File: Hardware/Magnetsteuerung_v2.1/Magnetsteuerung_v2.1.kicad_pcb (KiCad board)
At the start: 2 copper layers, 92.1 x 100.1 mm, 222 parts, among them J1 Conn_02x08_Odd_Even, J16 OUT1, J17 OUT1, J18 OUT1, J19 OUT1, J2 OUT1, J20 OUT1, J21 OUT1, J3 Conn_01x16, J4 OUT1, J5 OUT1, J6 OUT1, J7 OUT1, J8 OUT1, J9 Conn_01x16, Q1 Q_NMOS_GSD, Q10 Q_NMOS_GSD, Q11 Q_NMOS_GSD, Q12 Q_NMOS_GSD, Q13 Q_NMOS_GSD, Q14 Q_NMOS_GSD, Q15 Q_NMOS_GSD, Q16 Q_NMOS_GSD, Q17 Q_NMOS_GDS, Q2 Q_NMOS_GSD, Q3 Q_NMOS_GSD, Q4 Q_NMOS_GSD, Q5 Q_NMOS_GSD, Q6 Q_NMOS_GSD, Q7 Q_NMOS_GSD, Q8 Q_NMOS_GSD, U1 TL2575, U10 MCP1416R, U11 MCP1416R, U12 MCP1416R, U13 MCP1416R, U14 MCP1416R, U15 MCP1416R, U16 MCP1416R, U17 MCP1416R, U2 MCP1416R, U3 MCP1416R, U4 MCP1416R, U5 MCP1416R, U6 MCP1416R, U7 MCP1416R, U8 MCP1416R, U9 MCP1416R

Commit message: Add V2.1
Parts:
- removed D32, D33, D34, D41, D42, D43, D48, D49: LED, LED_SMD:LED_0603_1608Metric
- removed F10, F11, F12, F13, F14, F15, F16, F9: Fuse, Fuse:Fuse_2920_7451Metric_Pad2.10x5.45mm_HandSolder
- removed J16, J17, J18, J19, J20, J21, J5, J6: OUT1, MK_Footprints:SPTAF_2
- removed R42, R43, R44, R54, R55, R56, R63, R64: 9.5k, Resistor_SMD:R_0603_1608Metric
- added C10: 10u, Capacitor_SMD:C_1210_3225Metric, F.Cu at (171.1, 81.0)
- added C11: 10u, Capacitor_SMD:C_1210_3225Metric, F.Cu at (171.1, 111.5)
- added C12: 10u, Capacitor_SMD:C_1210_3225Metric, F.Cu at (171.1, 60.7)
- added C15: 10u, Capacitor_SMD:C_1210_3225Metric, F.Cu at (171.1, 91.2)
- C28, C29, C3, C30, C31, C32, C33, C34, C35, C36, C37, C38, C39, C40, C41, C42, C43, U1, U10, U11, U12, U13, U14, U15, U16, U17: moved to F.Cu
- C4, C5, C6, C7: value 100n -> 10u; footprint Capacitor_SMD:C_1206_3216Metric -> Capacitor_SMD:C_1210_3225Metric; moved to F.Cu
- R10, R19, R20, R21, R29, R3, R30, R39, R40, R41, R51, R52, R53, R61, R62, R9: value 10 -> 100
- R14, R16, R18, R26, R28, R34, R36, R38, R46, R48, R50, R58, R6, R60, R8: value 80 -> 10k
- R65, R66, R67, R68, R69, R70, R71, R72, R73, R74, R75, R76, R77, R78, R79, R80: value 3.3k -> 10k
- moved C7 68.2 mm to (171.1, 50.5)
- moved C6 26.6 mm to (171.1, 101.3)
- moved C5 24.9 mm to (171.1, 70.8)
- moved C4 24.6 mm to (169.6, 40.4)
- moved J4 19.2 mm to (156.5, 128.0), turned to 90 degrees
- moved J7 19.2 mm to (113.5, 34.0), turned to 270 degrees
- moved C1 18.5 mm to (126.6, 35.0)
- moved D26 18.4 mm to (157.4, 49.7)
- moved R73 18.4 mm to (154.4, 49.7)
- moved D35 17.8 mm to (157.4, 59.8)
- moved R76 17.8 mm to (154.4, 59.8)
- moved D44 17.3 mm to (157.4, 70.0)
- moved R79 17.3 mm to (154.4, 70.0)
- moved D27 16.8 mm to (157.4, 80.2)
- moved R74 16.8 mm to (154.4, 80.2)
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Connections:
- C4 pad 1: +12V -> GND
- C4 pad 2: GND -> +48V
- C5 pad 1: +12V -> GND
- C5 pad 2: GND -> +48V
- C6 pad 1: +12V -> GND
- C6 pad 2: GND -> +48V
- C7 pad 1: +12V -> GND
- C7 pad 2: GND -> +48V
- D29 pad 1: Net-(D29-Pad1) -> +48V
- D29 pad 2: Net-(D29-Pad2) -> OUT_9
- D30 pad 1: Net-(D30-Pad1) -> +48V
- D30 pad 2: Net-(D30-Pad2) -> OUT_12
- D31 pad 1: Net-(D31-Pad1) -> +48V
- D31 pad 2: Net-(D31-Pad2) -> OUT_15
- D38 pad 1: Net-(D38-Pad1) -> +48V
- D38 pad 2: Net-(D38-Pad2) -> OUT_10
- D39 pad 1: Net-(D39-Pad1) -> +48V
- D39 pad 2: Net-(D39-Pad2) -> OUT_13
- D40 pad 1: Net-(D40-Pad1) -> +48V
- D40 pad 2: Net-(D40-Pad2) -> OUT_16
- D46 pad 1: Net-(D46-Pad1) -> +48V
- D46 pad 2: Net-(D46-Pad2) -> OUT_11
- D47 pad 1: Net-(D47-Pad1) -> +48V
- D47 pad 2: Net-(D47-Pad2) -> OUT_14
- J9 pad 1: (no net) -> OUT_16
- J9 pad 10: (no net) -> +48V
- J9 pad 11: (no net) -> OUT_11
- J9 pad 12: (no net) -> +48V
- J9 pad 13: (no net) -> OUT_10
- J9 pad 14: (no net) -> +48V
- J9 pad 15: (no net) -> OUT_9
- J9 pad 16: (no net) -> +48V
- J9 pad 2: (no net) -> +48V
- J9 pad 3: (no net) -> OUT_15
- J9 pad 4: (no net) -> +48V
- J9 pad 5: (no net) -> OUT_14
- J9 pad 6: (no net) -> +48V
- J9 pad 7: (no net) -> OUT_13
- J9 pad 8: (no net) -> +48V
- J9 pad 9: (no net) -> OUT_12
- Q10 pad 2: Net-(D30-Pad2) -> OUT_12
- Q11 pad 2: Net-(D31-Pad2) -> OUT_15
- Q12 pad 2: Net-(D38-Pad2) -> OUT_10
- Q13 pad 2: Net-(D39-Pad2) -> OUT_13
- Q14 pad 2: Net-(D40-Pad2) -> OUT_16
- Q15 pad 2: Net-(D46-Pad2) -> OUT_11
- Q16 pad 2: Net-(D47-Pad2) -> OUT_14
- Q17 pad 2: Net-(D29-Pad2) -> OUT_9
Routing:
- net GND: track 211.1 -> 305.9 mm, vias 118 -> 0
- net IN8: track 12.3 -> 65.7 mm
- net IN7: track 12.3 -> 58.9 mm
- net IN6: track 12.3 -> 51.9 mm
- net IN5: track 12.3 -> 46.2 mm
- net IN4: track 12.3 -> 39.1 mm
- net Net-(D47-Pad1): track 26.2 -> 0.00 mm, vias 1 -> 0
- net Net-(D38-Pad1): track 26.1 -> 0.00 mm, vias 1 -> 0
- net Net-(D46-Pad1): track 26.1 -> 0.00 mm, vias 1 -> 0
- net Net-(D29-Pad1): track 26.1 -> 0.00 mm, vias 1 -> 0
- net Net-(D40-Pad1): track 26.0 -> 0.00 mm, vias 1 -> 0
- net Net-(D39-Pad1): track 26.0 -> 0.00 mm, vias 1 -> 0
- net Net-(D30-Pad1): track 26.0 -> 0.00 mm, vias 1 -> 0
- net Net-(D31-Pad1): track 26.0 -> 0.00 mm, vias 1 -> 0
- net Net-(R45-Pad1): track 29.2 -> 4.37 mm, vias 1 -> 0
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- added copper zone on B.Cu, net +12V
- removed copper zone on B.Cu, net GND
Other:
- rule trace_min: 0.2 -> 0

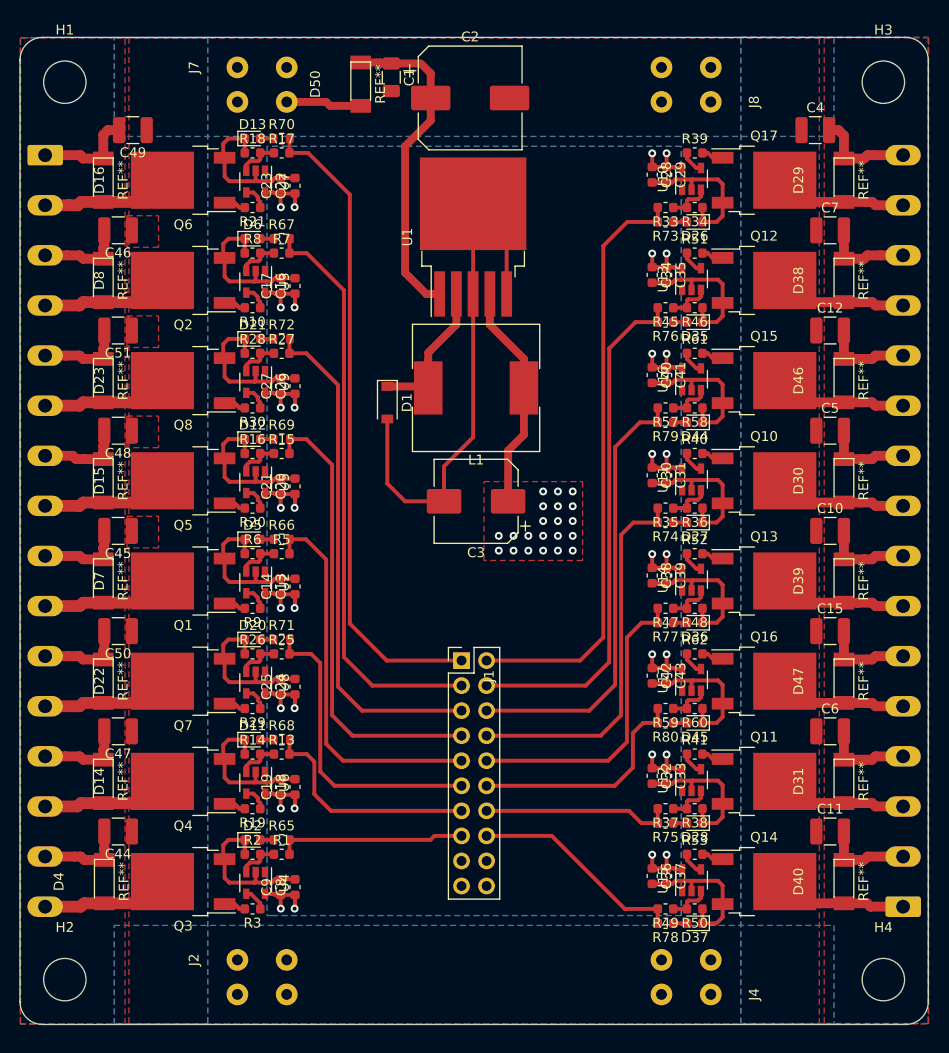
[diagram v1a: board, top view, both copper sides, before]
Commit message: update HW, supply over mounting hole
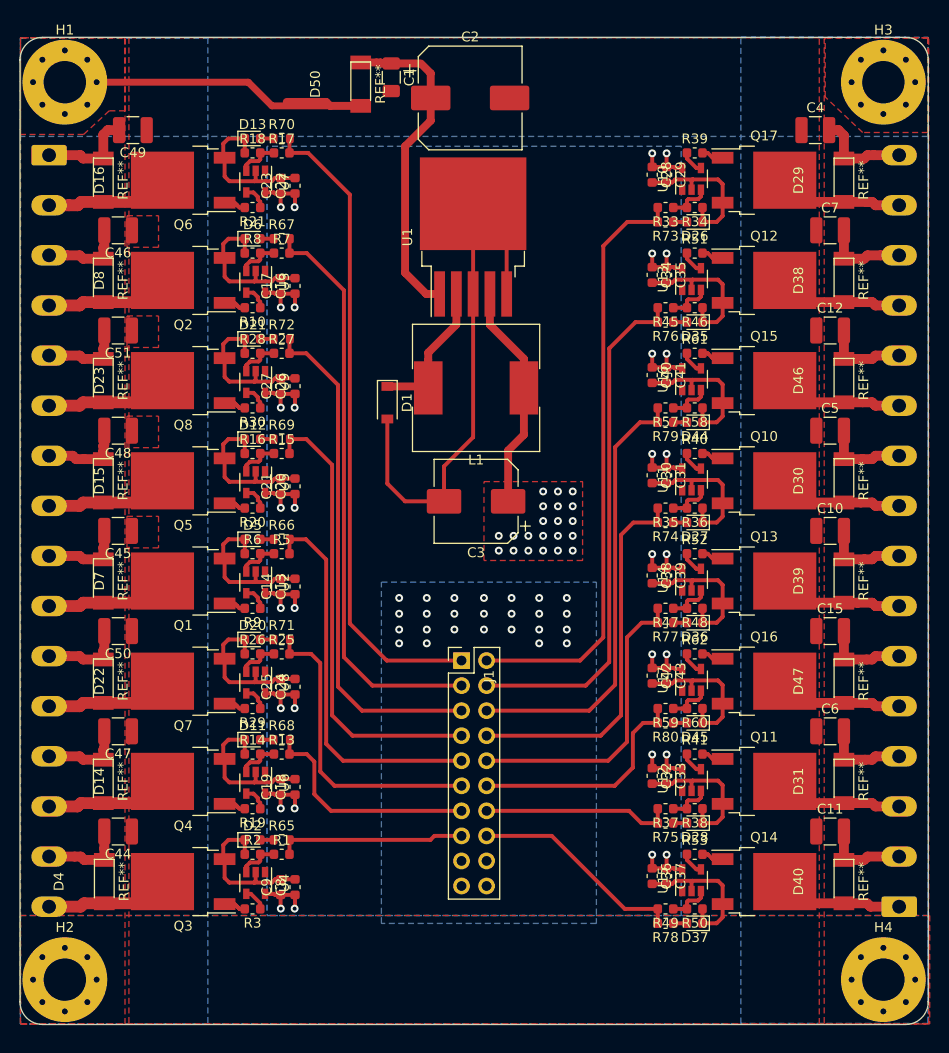
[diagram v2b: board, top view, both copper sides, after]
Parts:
- removed J2, J4, J7, J8: OUT1, MK_Footprints:SPTAF_2
- D1: value 1N5819 -> STPS2H100ZF
- H1, H2, H3, H4: footprint MountingHole:MountingHole_4.3mm_M4 -> MountingHole:MountingHole_4.3mm_M4_Pad_Via
- moved J3 0.40 mm to (91.9, 42.9)
- moved J9 0.40 mm to (178.1, 119.1)
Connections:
- H1 pad 1: (no net) -> +48V
- H2 pad 1: (no net) -> GND
- H3 pad 1: (no net) -> +48V
- H4 pad 1: (no net) -> GND
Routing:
- net +48V: track 154.1 -> 185.1 mm
- net GND: vias 0 -> 25
- added copper zone on B.Cu, net GND

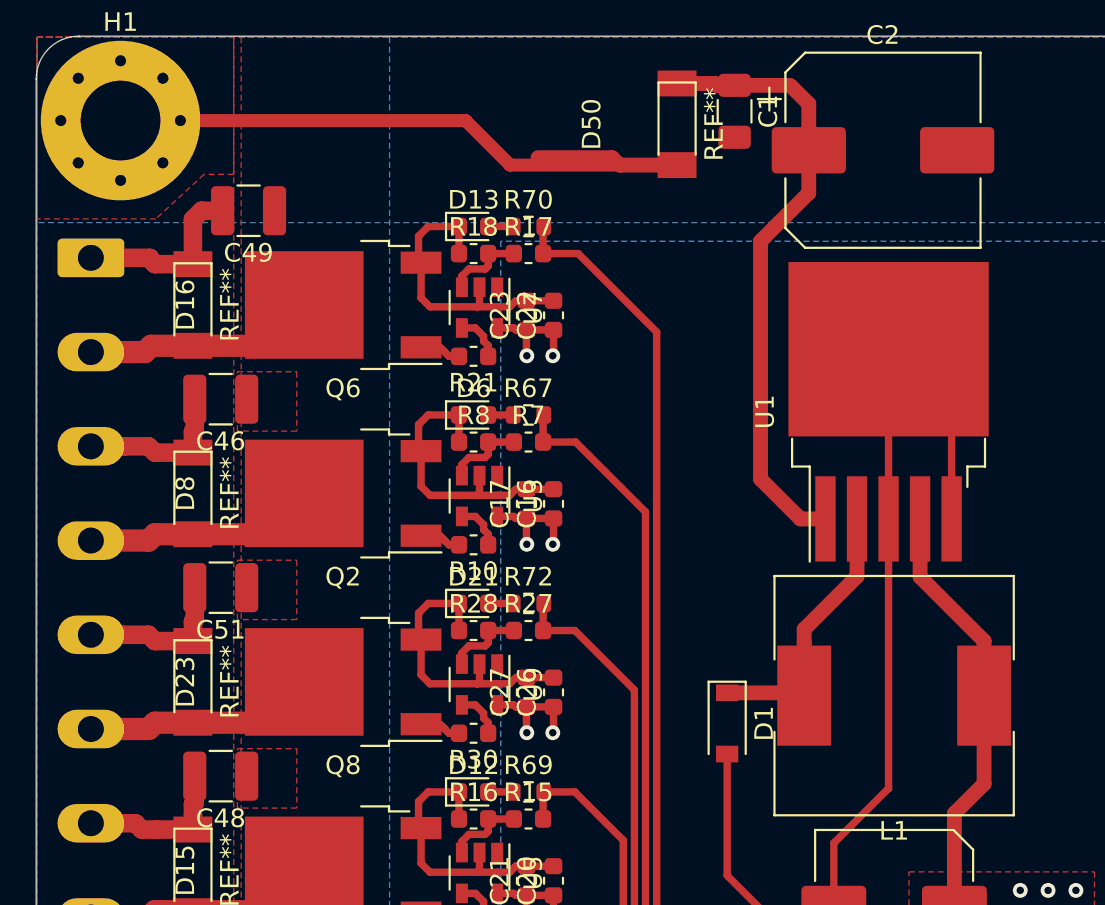
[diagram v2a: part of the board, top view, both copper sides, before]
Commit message: Change wire thiknes
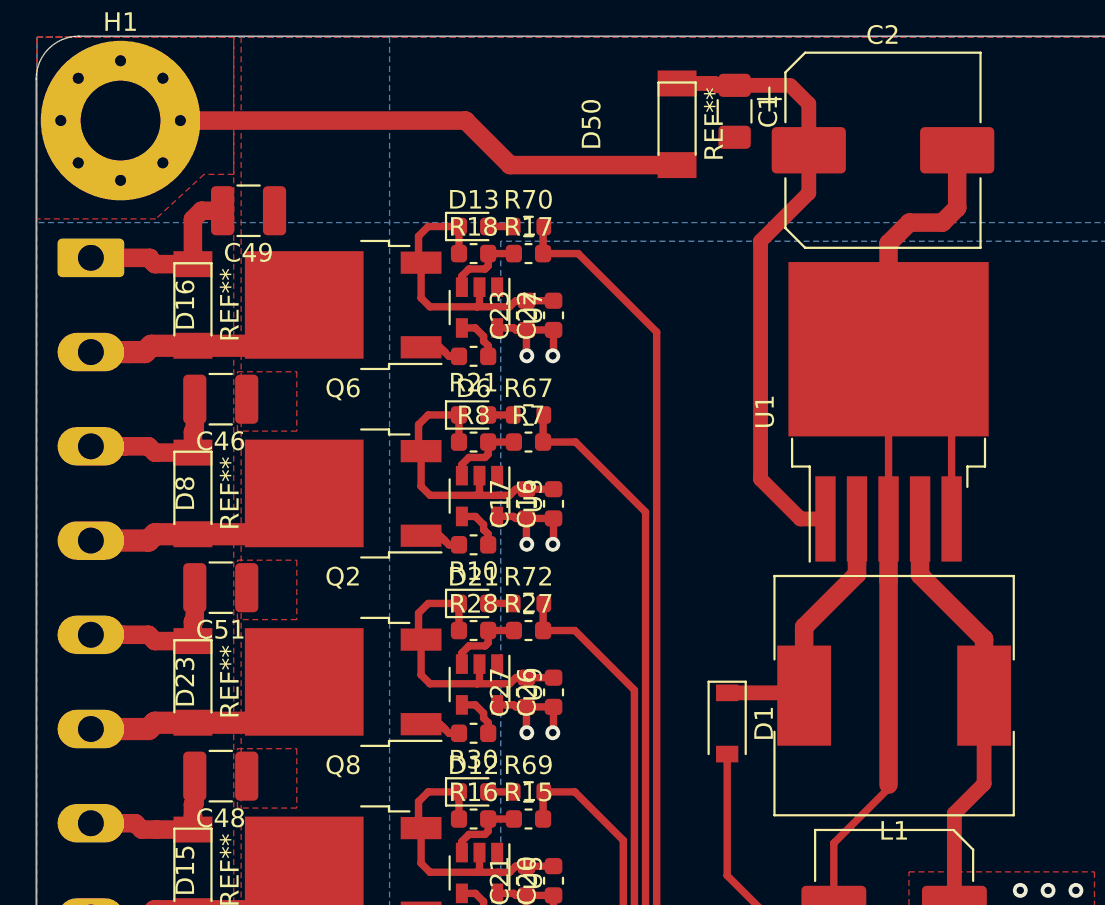
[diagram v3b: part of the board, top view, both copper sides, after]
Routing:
- net GND: track 305.9 -> 319.2 mm
- net +48V: track 185.1 -> 177.4 mm
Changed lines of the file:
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@@
     (thickness 1.6)
     (drawings 31)
-    (tracks 989)
+    (tracks 993)
     (zones 0)
     (modules 190)
@@
   )
   (setup
-    (last_trace_width 0.7)
+    (last_trace_width 1)
     (user_trace_width 0.4)
     (user_trace_width 0.5)
@@
   (gr_line (start 181.05 128.75) (end 181.05 33.25) (layer Edge.Cuts) (width 0.05))
   (gr_line (start 91.25 131.05) (end 178.75 131.05) (layer Edge.Cuts) (width 0.05))
-  (via (at 144.4 87.8) (size 0.8) (drill 0.4) (layers F.Cu B.Cu) (net 3))
-  (via (at 138.8 87.8) (size 0.8) (drill 0.4) (layers F.Cu B.Cu) (net 3))
-  (via (at 141.6 87.8) (size 0.8) (drill 0.4) (layers F.Cu B.Cu) (net 3))
-  (via (at 136 87.8) (size 0.8) (drill 0.4) (layers F.Cu B.Cu) (net 3))
-  (via (at 133 87.8) (size 0.8) (drill 0.4) (layers F.Cu B.Cu) (net 3))
   (segment (start 111.7425 88.85) (end 111.205 88.85) (width 0.4) (layer F.Cu) (net 1))
   (segment (start 109.7 88.36) (end 110.715 88.36) (width 0.4) (layer F.Cu) (net 1))
@@
   (segment (start 172.5 101.32) (end 172.5 104.2) (width 1) (layer F.Cu) (net 2))
   (segment (start 172.5 111.48) (end 172.5 114.36) (width 1) (layer F.Cu) (net 2))
-  (segment (start 120 37.5) (end 120.4 37.9) (width 0.8) (layer F.Cu) (net 2))
-  (segment (start 116 37.5) (end 120 37.5) (width 0.8) (layer F.Cu) (net 2))
-  (segment (start 123.5 37.9) (end 120.4 37.9) (width 0.8) (layer F.Cu) (net 2))
-  (segment (start 123.5 37.9) (end 114.5 37.9) (width 0.7) (layer F.Cu) (net 2))
-  (segment (start 112.1 35.5) (end 93.5 35.5) (width 0.7) (layer F.Cu) (net 2))
-  (segment (start 114.5 37.9) (end 112.1 35.5) (width 0.7) (layer F.Cu) (net 2))
+  (segment (start 123.5 37.9) (end 114.5 37.9) (width 1) (layer F.Cu) (net 2))
+  (segment (start 112.1 35.5) (end 93.5 35.5) (width 1) (layer F.Cu) (net 2))
+  (segment (start 114.5 37.9) (end 112.1 35.5) (width 1) (layer F.Cu) (net 2))
+  (via (at 144.4 87.8) (size 0.8) (drill 0.4) (layers F.Cu B.Cu) (net 3))
+  (via (at 138.8 87.8) (size 0.8) (drill 0.4) (layers F.Cu B.Cu) (net 3))
+  (via (at 141.6 87.8) (size 0.8) (drill 0.4) (layers F.Cu B.Cu) (net 3))
+  (via (at 136 87.8) (size 0.8) (drill 0.4) (layers F.Cu B.Cu) (net 3))
+  (via (at 133 87.8) (size 0.8) (drill 0.4) (layers F.Cu B.Cu) (net 3))
   (segment (start 157.16 106.32) (end 157.05 106.43) (width 0.4) (layer F.Cu) (net 3))
   (segment (start 160.2 110.02) (end 160.2 108.68) (width 0.4) (layer F.Cu) (net 3))
@@
   (segment (start 138.3 56.975) (end 138.3 51.225) (width 0.4) (layer F.Cu) (net 3))
   (segment (start 131.95 74.45) (end 131.95 78) (width 0.4) (layer F.Cu) (net 3))
-  (segment (start 134.9 56.975) (end 134.9 71.5) (width 0.4) (layer F.Cu) (net 3))
   (segment (start 134.9 71.5) (end 131.95 74.45) (width 0.4) (layer F.Cu) (net 3))
   (segment (start 126.2 69.65) (end 126.2 76.2) (width 0.4) (layer F.Cu) (net 3))
@@
   (via (at 127.4 87.8) (size 0.8) (drill 0.4) (layers F.Cu B.Cu) (net 3))
   (via (at 130.2 87.8) (size 0.8) (drill 0.4) (layers F.Cu B.Cu) (net 3))
+  (segment (start 134.9 60.275) (end 134.9 71.3) (width 1) (layer F.Cu) (net 3))
+  (segment (start 134.9 56.975) (end 134.9 60.275) (width 1) (layer F.Cu) (net 3))
+  (segment (start 134.9 71.3) (end 134.9 71.5) (width 0.4) (layer F.Cu) (net 3))
+  (segment (start 134.9 42.125) (end 136.025 41) (width 1) (layer F.Cu) (net 3))
+  (segment (start 134.9 47.825) (end 134.9 42.125) (width 1) (layer F.Cu) (net 3))
+  (segment (start 136.025 41) (end 137.8 41) (width 1) (layer F.Cu) (net 3))
+  (segment (start 138.6 40.2) (end 138.6 37.1) (width 1) (layer F.Cu) (net 3))
+  (segment (start 137.8 41) (end 138.6 40.2) (width 1) (layer F.Cu) (net 3))
   (segment (start 111.7425 58.37) (end 111.205 58.37) (width 0.4) (layer F.Cu) (net 4))
   (segment (start 109.7 57.88) (end 110.715 57.88) (width 0.4) (layer F.Cu) (net 4))
@@
   (via (at 153.06 42.71) (size 0.8) (drill 0.4) (layers F.Cu B.Cu) (net 17))
   (segment (start 154.52 44.0925) (end 154.52 42.71) (width 0.4) (layer F.Cu) (net 17))
-  (segment (start 136.6 60.1) (end 140.05 63.55) (width 0.8) (layer F.Cu) (net 17))
-  (segment (start 136.6 56.975) (end 136.6 60.1) (width 0.8) (layer F.Cu) (net 17))
-  (segment (start 140.05 63.55) (end 140.05 66.5) (width 0.8) (layer F.Cu) (net 17))
   (segment (start 138.45 72.85) (end 140.05 71.25) (width 0.8) (layer F.Cu) (net 17))
   (segment (start 138.45 78) (end 138.45 72.85) (width 0.8) (layer F.Cu) (net 17))
@@
   (via (at 139 83) (size 0.8) (drill 0.4) (layers F.Cu B.Cu) (net 17))
   (via (at 140.5 83) (size 0.8) (drill 0.4) (layers F.Cu B.Cu) (net 17))
+  (segment (start 140.05 63.45) (end 140.05 66.5) (width 1) (layer F.Cu) (net 17))
+  (segment (start 136.6 56.975) (end 136.6 60) (width 1) (layer F.Cu) (net 17))
+  (segment (start 136.6 60) (end 140.05 63.45) (width 1) (layer F.Cu) (net 17))
   (segment (start 126.25 66.5) (end 126.2 66.45) (width 0.4) (layer F.Cu) (net 18))
   (segment (start 130.35 66.5) (end 126.25 66.5) (width 0.4) (layer F.Cu) (net 18))
-  (segment (start 130.35 62.925) (end 130.35 63.65) (width 0.8) (layer F.Cu) (net 18))
-  (segment (start 133.2 60.075) (end 130.35 62.925) (width 0.8) (layer F.Cu) (net 18))
-  (segment (start 133.2 56.975) (end 133.2 60.075) (width 0.8) (layer F.Cu) (net 18))
-  (segment (start 130.35 63.65) (end 130.35 66.5) (width 0.8) (layer F.Cu) (net 18))
   (segment (start 130.2 66.35) (end 130.35 66.5) (width 0.8) (layer F.Cu) (net 18))
   (segment (start 126.2 66.35) (end 130.2 66.35) (width 0.8) (layer F.Cu) (net 18))
+  (segment (start 133.2 59.95) (end 133.2 59.4) (width 1) (layer F.Cu) (net 18))
+  (segment (start 130.35 62.8) (end 133.2 59.95) (width 1) (layer F.Cu) (net 18))
+  (segment (start 130.35 66.5) (end 130.35 62.8) (width 1) (layer F.Cu) (net 18))
+  (segment (start 133.2 56.975) (end 133.2 59.4) (width 1) (layer F.Cu) (net 18))
   (segment (start 111.9 54.64) (end 111.9 54.04) (width 0.4) (layer F.Cu) (net 19))
   (segment (start 111.9 54.04) (end 112.28 53.66) (width 0.4) (layer F.Cu) (net 19))

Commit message: fertigungsdaten aufbereitet
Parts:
- removed D50: PMEG6010CEH, MK_Footprints:D_SOD_128_2
- added C52: 100u, Capacitor_SMD:CP_Elec_10x10, F.Cu at (145.9, 37.6)
- added C53: 100u, Capacitor_SMD:CP_Elec_10x10, F.Cu at (123.9, 37.6)
- added C55: 100n, Capacitor_SMD:C_1206_3216Metric, F.Cu at (125.5, 56.8)
- moved C1 21.8 mm to (127.8, 56.8), turned to 90 degrees
- moved U1 1.20 mm to (134.9, 52.4)
- moved L1 1.00 mm to (135.2, 67.5)
- moved C2 0.58 mm to (134.9, 37.6), turned to 270 degrees
- moved C3 0.50 mm to (135.2, 78.5)
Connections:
- C1 pad 1: Net-(C1-Pad1) -> +48V
- C2 pad 1: Net-(C1-Pad1) -> +48V
- U1 pad 1: Net-(C1-Pad1) -> +48V
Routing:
- net Net-(C1-Pad1): track 33.2 -> 0.00 mm
- net GND: track 319.2 -> 305.9 mm
- net +48V: track 177.4 -> 184.0 mm
- net Net-(D1-Pad1): track 19.1 -> 21.3 mm
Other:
- board text added: "Pamatech System AG"
- board text added: "SN4855S24A8"
- board text added: "Vin: 48-55V"
- board text removed: "+48V"

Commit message: change hardware
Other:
- net class Default removed

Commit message: Finalisierung
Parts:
- C2, C52, C53: footprint Capacitor_SMD:CP_Elec_10x10 -> Capacitor_SMD:CP_Elec_10x10.5
- D14, D15, D16, D22, D23, D7, D8: footprint MK_Footprints:SOD_128 -> MK_Footprints:D_SOD_128_2
- Q17: value Q_NMOS_GDS -> Q_NMOS_GSD
- moved U1 0.14 mm to (134.9, 52.5)
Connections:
- J1 pad 17: (no net) -> unconnected-(J1-Pin_17-Pad17)
- J1 pad 19: (no net) -> unconnected-(J1-Pin_19-Pad19)
- U10 pad 1: (no net) -> unconnected-(U10-NC-Pad1)
- U11 pad 1: (no net) -> unconnected-(U11-NC-Pad1)
- U12 pad 1: (no net) -> unconnected-(U12-NC-Pad1)
- U13 pad 1: (no net) -> unconnected-(U13-NC-Pad1)
- U14 pad 1: (no net) -> unconnected-(U14-NC-Pad1)
- U15 pad 1: (no net) -> unconnected-(U15-NC-Pad1)
- U16 pad 1: (no net) -> unconnected-(U16-NC-Pad1)
- U17 pad 1: (no net) -> unconnected-(U17-NC-Pad1)
- U2 pad 1: (no net) -> unconnected-(U2-NC-Pad1)
- U3 pad 1: (no net) -> unconnected-(U3-NC-Pad1)
- U4 pad 1: (no net) -> unconnected-(U4-NC-Pad1)
- U5 pad 1: (no net) -> unconnected-(U5-NC-Pad1)
- U6 pad 1: (no net) -> unconnected-(U6-NC-Pad1)
- U7 pad 1: (no net) -> unconnected-(U7-NC-Pad1)
- U8 pad 1: (no net) -> unconnected-(U8-NC-Pad1)
- U9 pad 1: (no net) -> unconnected-(U9-NC-Pad1)
